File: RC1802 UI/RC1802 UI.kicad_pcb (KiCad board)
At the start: 2 copper layers, 99.1 x 99.1 mm, 65 parts, among them J1 CONN_01X39, J2 BARREL_JACK, J3 Mount, J4 Mount, J5 Mount, J6 Mount, SW1 CLEAR, SW10 IN5, SW11 IN6, SW12 IN7, SW2 IN, SW3 MP, SW4 WAIT, SW5 IN0, SW6 IN1, SW7 IN2, SW8 IN3, SW9 IN4, U1 CDP1802, U10 MC14495P1, U11 28C256, U2 74LS373, U3 HM62256BLP-7, U4 74LS04, U5 4050, U6 4013, U7 74LS10, U8 MC14495P1, U9 74LS245, X1 CXO_DIP14

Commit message: Completed front panel with exports.
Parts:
- removed C10, C11, C8, C9: 100nF, Capacitors_THT:C_Disc_D4.7mm_W2.5mm_P5.00mm
- removed JP1: U12 WE, Pin_Headers:Pin_Header_Straight_1x03_Pitch2.54mm
- removed JP2: Enable, Pin_Headers:Pin_Header_Straight_1x02_Pitch2.54mm
- removed JP3: HI, Pin_Headers:Pin_Header_Straight_1x03_Pitch2.54mm
- removed JP4: LO, Pin_Headers:Pin_Header_Straight_1x03_Pitch2.54mm
- removed R10: 470, Resistors_THT:R_Axial_DIN0207_L6.3mm_D2.5mm_P10.16mm_Horizontal
- removed R4, R5, R6, R7, R8, R9: 47k, Resistors_THT:R_Axial_DIN0207_L6.3mm_D2.5mm_P10.16mm_Horizontal
- removed U10, U8: MC14495P1, Housings_DIP:DIP-16_W7.62mm_Socket
- removed U11: 28C256, Housings_DIP:DIP-32_W15.24mm_Socket
- removed U9: 74LS245, Housings_DIP:DIP-20_W7.62mm_Socket
- removed X1: CXO_DIP14, Oscillators:Oscillator_DIP-14
- J1: value CONN_01X39 -> Mount; footprint Pin_Headers:Pin_Header_Angled_1x39_Pitch2.54mm -> mounting:1pin
- J2: value BARREL_JACK -> Mount; footprint Connectors:BARREL_JACK -> mounting:1pin
- J5: value Mount -> CONN_01X39; footprint mounting:1pin -> Pin_Headers:Pin_Header_Angled_1x39_Pitch2.54mm
- J6: value Mount -> CONN_02X20; footprint mounting:1pin -> Connectors:IDC_Header_Straight_40pins
- R1: value 47k -> 470
- U1: value CDP1802 -> 74LS04; footprint Housings_DIP:DIP-40_W15.24mm_Socket -> Housings_DIP:DIP-14_W7.62mm_Socket
- U2: value 74LS373 -> 4050; footprint Housings_DIP:DIP-20_W7.62mm_Socket -> Housings_DIP:DIP-16_W7.62mm_Socket
- U3: value HM62256BLP-7 -> 4013; footprint Housings_DIP:DIP-32_W15.24mm_Socket -> Housings_DIP:DIP-14_W7.62mm_Socket
- U4: value 74LS04 -> 74LS10
- U5: value 4050 -> MC14495P1
- U6: value 4013 -> 74LS245; footprint Housings_DIP:DIP-14_W7.62mm_Socket -> Housings_DIP:DIP-20_W7.62mm_Socket
- U7: value 74LS10 -> MC14495P1; footprint Housings_DIP:DIP-14_W7.62mm_Socket -> Housings_DIP:DIP-16_W7.62mm_Socket
- moved D4 248.7 mm to (121.3, 101.6), turned to 180 degrees
- moved R1 221.3 mm to (144.8, 107.3), turned to 180 degrees
- moved R3 198.4 mm to (182.2, 123.8), turned to 90 degrees
- moved D3 195.1 mm to (186.1, 113.7), turned to 270 degrees
- moved D6 194.2 mm to (121.3, 104.1), turned to 180 degrees
- moved D2 189.6 mm to (191.8, 113.7), turned to 270 degrees
- moved D7 163.2 mm to (195.6, 113.7), turned to 270 degrees
- moved D5 160.9 mm to (121.3, 99.1), turned to 180 degrees
- moved J5 132.0 mm to (198.1, 146.1), turned to 270 degrees
- moved J6 118.2 mm to (107.3, 132.1), turned to 90 degrees
- moved SW5 112.3 mm to (194.3, 131.4), turned to 270 degrees
- moved J2 108.4 mm to (104.8, 71.8)
- moved SW3 103.8 mm to (117.5, 131.4), turned to 270 degrees
- moved SW6 100.8 mm to (186.1, 131.4), turned to 270 degrees
- moved SW2 92.3 mm to (127.0, 131.4), turned to 270 degrees
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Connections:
- D3 pad 2: WAIT -> ~WAIT
- J1 pad 1: EF1 -> (no net)
- J2 pad 1: VCC -> (no net)
- R1 pad 1: INTERRUPT -> Net-(D1-Pad2)
- R2 pad 1: DMA_OUT -> GND
- R2 pad 2: VCC -> Net-(D3-Pad1)
- R3 pad 1: DMA_IN -> GND
- R3 pad 2: VCC -> LOAD_N2
- SW1 pad 2: CLEAR -> ~CLEAR
- SW3 pad 2: ~WE -> MP
- U1 pad 1: CLOCK -> Net-(D1-Pad1)
- U1 pad 10: /BUS5 -> Net-(D6-Pad2)
- U1 pad 11: /BUS4 -> ~WAIT
- U1 pad 12: /BUS3 -> (no net)
- U1 pad 13: /BUS2 -> (no net)
- U1 pad 14: /BUS1 -> VCC
- U1 pad 2: WAIT -> Q
- U1 pad 3: CLEAR -> Net-(SW2-Pad2)
- U1 pad 4: Q -> /~IN
- U1 pad 5: SC1 -> Net-(D6-Pad2)
- U1 pad 6: SC0 -> ~WAIT
- U1 pad 7: MRD -> GND
- U1 pad 8: /BUS7 -> Net-(SW2-Pad2)
- U1 pad 9: /BUS6 -> /~IN
- U2 pad 1: GND -> VCC
- U2 pad 10: GND -> (no net)
- U2 pad 11: TPA -> (no net)
- U2 pad 12: /MA12 -> (no net)
- U2 pad 13: /MA4 -> (no net)
- U2 pad 14: /MA5 -> (no net)
- U2 pad 15: /MA13 -> (no net)
- U2 pad 16: /MA14 -> (no net)
- U2 pad 2: /MA8 -> ~CLEAR
- U2 pad 3: /MA0 -> ~CLEAR
- U2 pad 4: /MA1 -> STROBE
- U2 pad 5: /MA9 -> Net-(U2-Pad5)
- U2 pad 6: /MA10 -> (no net)
- U2 pad 7: /MA2 -> (no net)
- U2 pad 8: /MA3 -> (no net)
- U2 pad 9: /MA11 -> (no net)
- U3 pad 1: /MA14 -> (no net)
- U3 pad 10: /MA0 -> Net-(D3-Pad1)
- U3 pad 11: /BUS0 -> /~IN
- U3 pad 12: /BUS1 -> Net-(D5-Pad1)
- U3 pad 13: /BUS2 -> (no net)
- U3 pad 14: GND -> VCC
- U3 pad 2: /MA12 -> (no net)
- U3 pad 3: /MA7 -> (no net)
- U3 pad 4: /MA6 -> (no net)
- U3 pad 5: /MA5 -> (no net)
- U3 pad 6: /MA4 -> (no net)
- U3 pad 7: /MA3 -> GND
- U3 pad 8: /MA2 -> GND
- U3 pad 9: /MA1 -> VCC
- U4 pad 1: Net-(D1-Pad1) -> MRD
- U4 pad 10: Net-(D6-Pad2) -> TPB
- U4 pad 11: WAIT -> Net-(U4-Pad11)
- U4 pad 12: Net-(JP3-Pad2) -> Net-(U4-Pad11)
- U4 pad 13: /MA15 -> MRD
- U4 pad 2: Q -> MRD
- U4 pad 3: Net-(SW2-Pad2) -> MRD
- U4 pad 4: /~IN -> LOAD_N2
- U4 pad 5: Net-(D6-Pad2) -> LOAD_N2
- U4 pad 6: WAIT -> READ
- U4 pad 8: Net-(SW2-Pad2) -> Net-(U2-Pad5)
- U4 pad 9: /~IN -> LOAD_N2
- U5 pad 1: VCC -> Net-(AFF1-Pad1)
- U5 pad 10: (no net) -> /BUS4
- U5 pad 12: (no net) -> Net-(AFF1-Pad7)
- U5 pad 13: (no net) -> Net-(AFF1-Pad6)
- U5 pad 14: (no net) -> Net-(AFF1-Pad4)
- U5 pad 15: (no net) -> Net-(AFF1-Pad2)
- U5 pad 16: (no net) -> VCC
- U5 pad 2: CLEAR -> Net-(AFF1-Pad9)
- U5 pad 3: CLEAR -> Net-(AFF1-Pad10)
- U5 pad 4: STROBE -> (no net)
- U5 pad 5: Net-(U5-Pad5) -> /BUS7
- U5 pad 6: (no net) -> /BUS6
- U5 pad 7: (no net) -> STROBE
- U5 pad 8: (no net) -> GND
- U5 pad 9: (no net) -> /BUS5
- U6 pad 1: (no net) -> VCC
- U6 pad 10: Net-(D3-Pad1) -> GND
- U6 pad 11: /~IN -> /BUS7
- U6 pad 12: Net-(D5-Pad1) -> /BUS6
- U6 pad 13: (no net) -> /BUS5
- U6 pad 14: VCC -> /BUS4
- U6 pad 2: (no net) -> Net-(SW5-Pad2)
- U6 pad 3: (no net) -> Net-(SW6-Pad2)
- U6 pad 4: (no net) -> Net-(SW7-Pad2)
- U6 pad 5: (no net) -> Net-(SW8-Pad2)
- U6 pad 6: (no net) -> Net-(SW9-Pad2)
- U6 pad 7: GND -> Net-(SW10-Pad2)
- U6 pad 8: GND -> Net-(SW11-Pad2)
- U6 pad 9: VCC -> Net-(SW12-Pad2)
- U7 pad 1: MRD -> Net-(AFF2-Pad1)
- U7 pad 10: TPB -> /BUS0
- U7 pad 11: Net-(U7-Pad11) -> (no net)
- U7 pad 12: Net-(U7-Pad11) -> Net-(AFF2-Pad7)
- U7 pad 13: MRD -> Net-(AFF2-Pad6)
- U7 pad 14: VCC -> Net-(AFF2-Pad4)
- U7 pad 2: MRD -> Net-(AFF2-Pad9)
- U7 pad 3: MRD -> Net-(AFF2-Pad10)
- U7 pad 4: LOAD_N2 -> (no net)
- U7 pad 5: LOAD_N2 -> /BUS3
- U7 pad 6: READ -> /BUS2
- U7 pad 7: GND -> STROBE
- U7 pad 8: Net-(U5-Pad5) -> GND
- U7 pad 9: LOAD_N2 -> /BUS1
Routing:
- net N2: track 18.4 -> 226.3 mm, vias 0 -> 5
- net ~WAIT: track 0.00 -> 199.1 mm, vias 0 -> 17
- net MRD: track 0.00 -> 196.3 mm, vias 0 -> 8
- net ~CLEAR: track 0.00 -> 182.5 mm, vias 0 -> 12
- net TPB: track 0.00 -> 173.5 mm, vias 0 -> 11
- net SC1: track 0.00 -> 147.3 mm, vias 0 -> 8
- net EF4: track 6.99 -> 153.7 mm, vias 2 -> 9
- net LOAD_N2: track 0.00 -> 133.8 mm, vias 0 -> 4
- net /~IN: track 0.00 -> 106.9 mm, vias 0 -> 7
- net MWR: track 0.00 -> 104.8 mm, vias 0 -> 3
- net Q: track 0.00 -> 101.8 mm, vias 0 -> 7
- net STROBE: track 0.00 -> 97.9 mm, vias 0 -> 6
- net Net-(D3-Pad1): track 0.00 -> 83.7 mm, vias 0 -> 5
- net Net-(SW6-Pad2): track 127.4 -> 50.0 mm, vias 3 -> 0
- net /MA11: track 76.0 -> 0.00 mm, vias 2 -> 0
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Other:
- board size 99.1 x 99.1 mm -> 99.1 x 80 mm
- board text added: "0"
- board text added: "1"
- board text added: "2"
- board text added: "3"
- board text added: "4"
- board text added: "5"
- board text added: "6"
- board text added: "7"
- board text added: "CLEAR"
- board text added: "Front panel connector"
- board text added: "IN"
- board text added: "MP"
- board text added: "RC1802 Cosmac ELF Revision A"
- board text added: "WAIT"

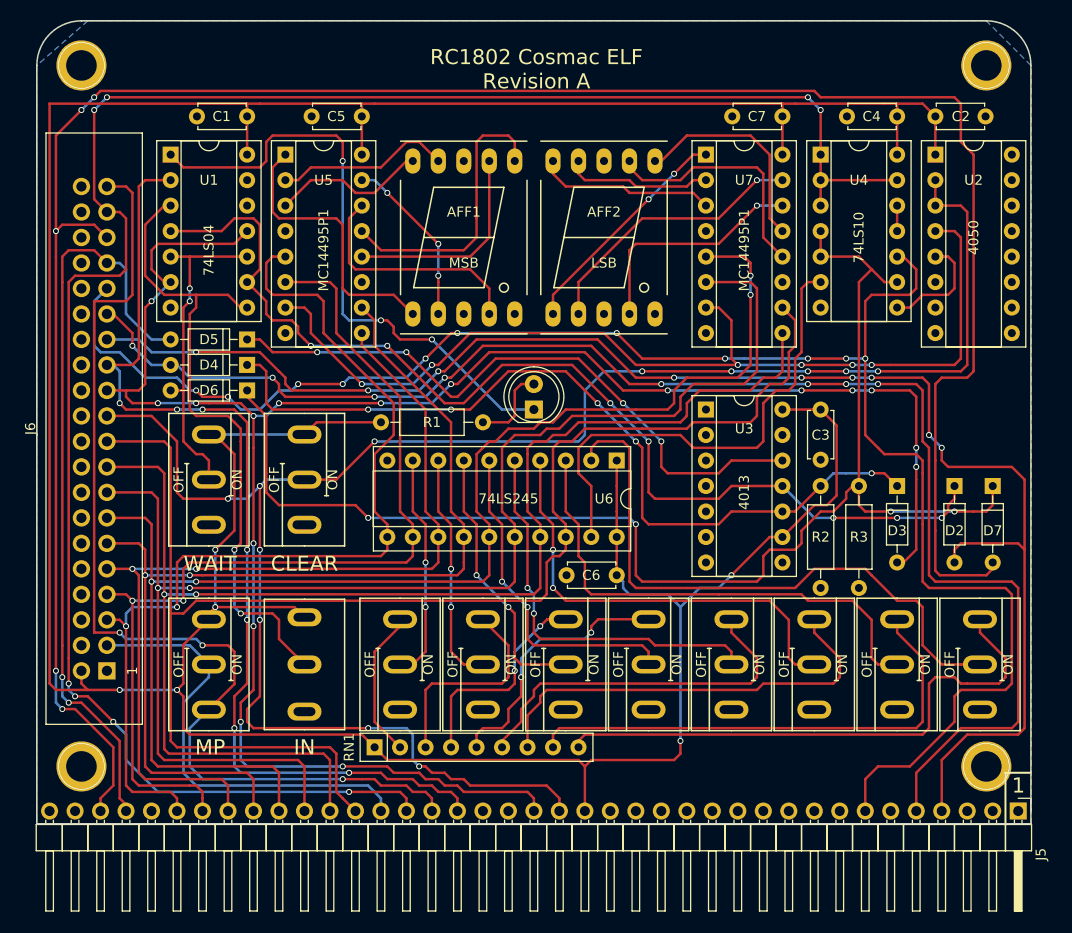
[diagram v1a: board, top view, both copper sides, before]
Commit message: Increased hole sizes for switches
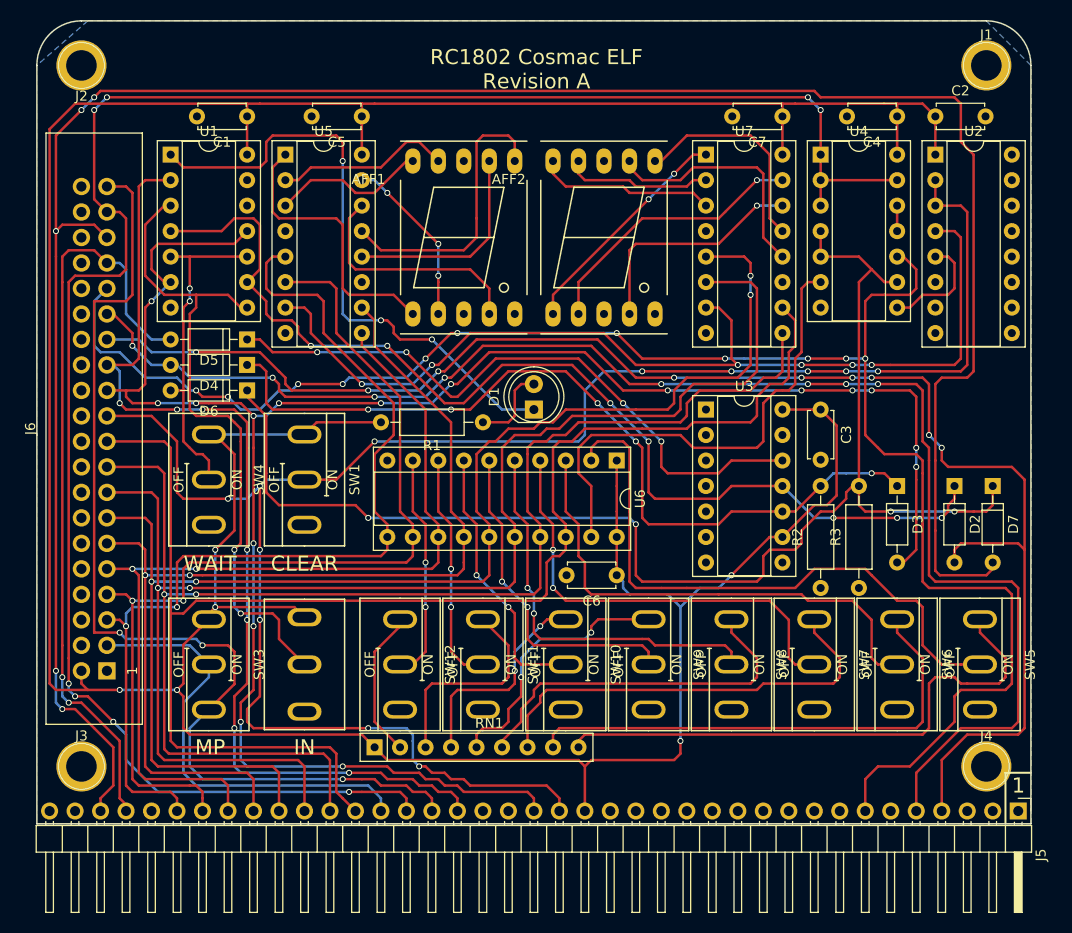
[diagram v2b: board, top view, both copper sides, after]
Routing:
- net VCC: track 370.1 -> 368.6 mm

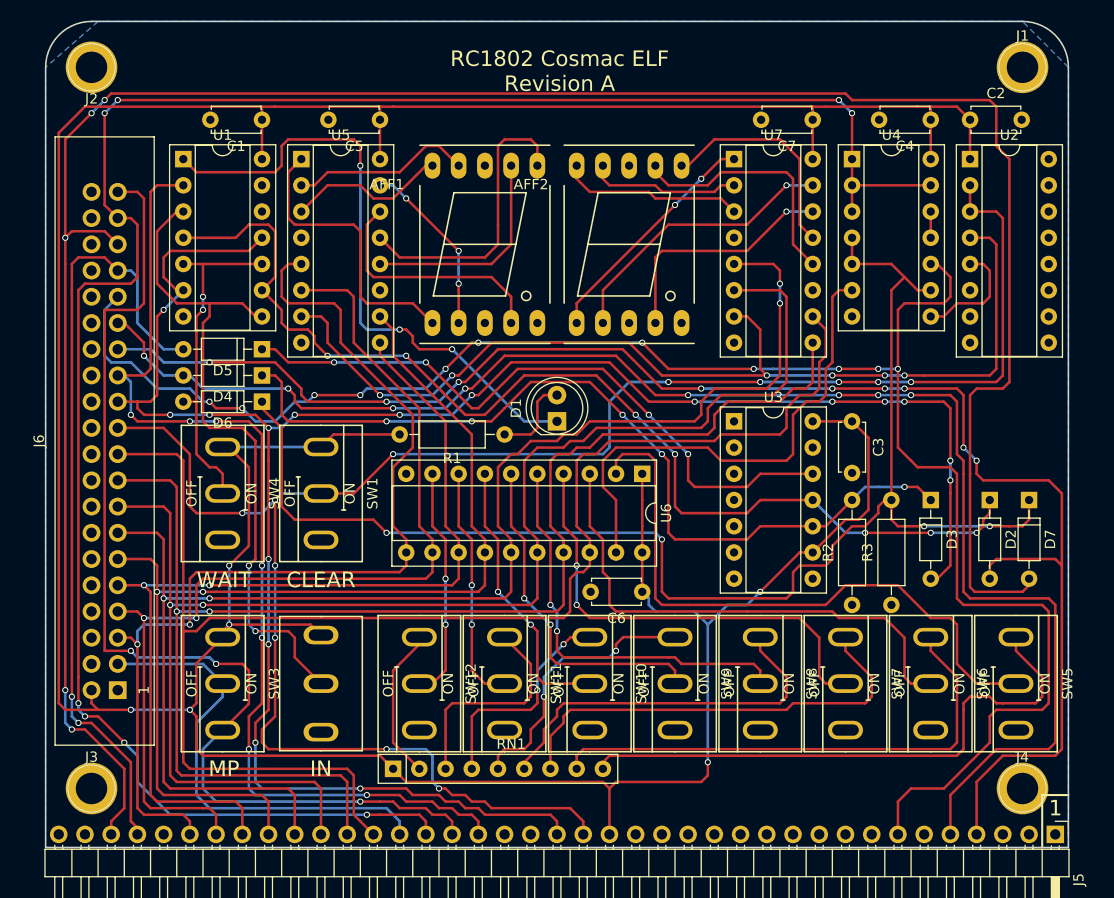
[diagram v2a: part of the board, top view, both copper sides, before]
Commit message: Silkscreen cleanup
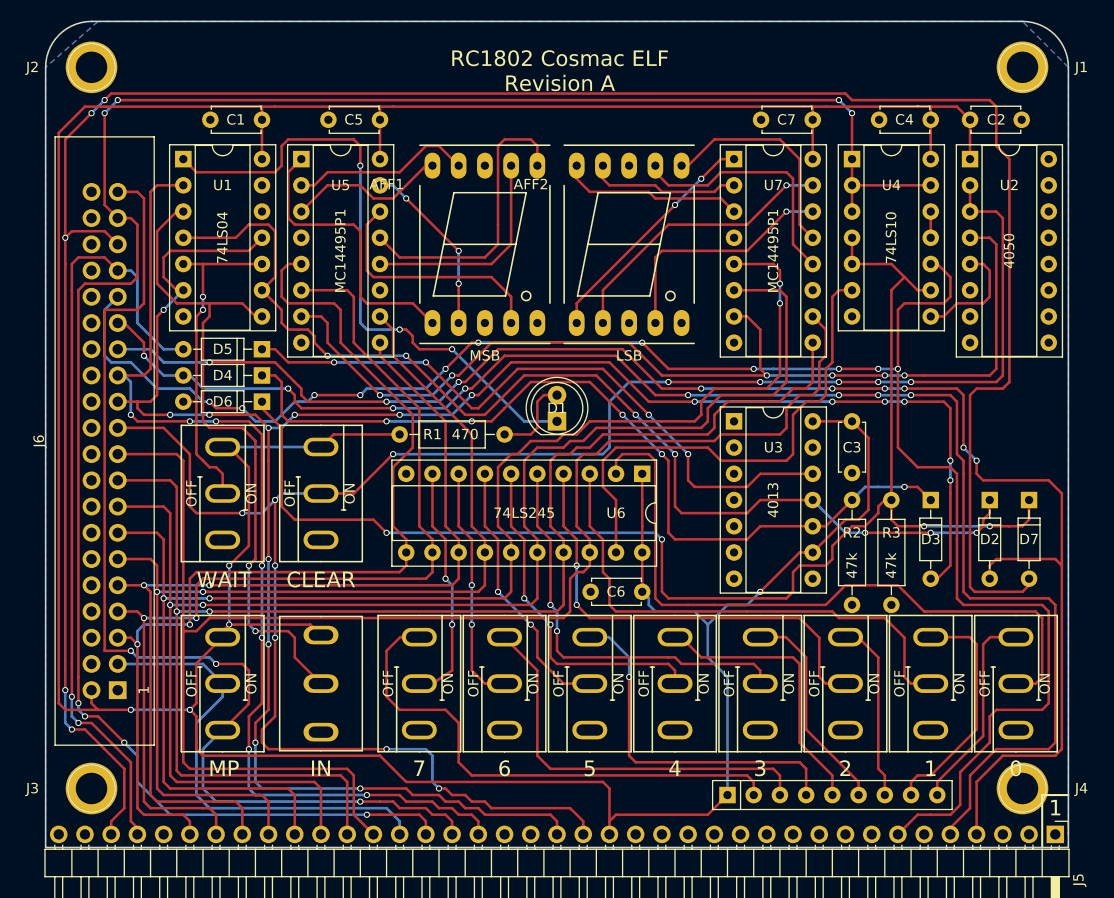
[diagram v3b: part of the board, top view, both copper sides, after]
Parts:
- moved RN1 32.5 mm to (166.4, 142.2)
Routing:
- net Net-(RN1-Pad2): track 14.9 -> 51.3 mm
- net Net-(RN1-Pad9): track 55.8 -> 19.9 mm
- net Net-(RN1-Pad8): track 49.9 -> 22.7 mm
- net Net-(RN1-Pad7): track 43.1 -> 17.6 mm
- net Net-(RN1-Pad3): track 21.3 -> 39.0 mm
- net Net-(RN1-Pad6): track 36.6 -> 20.7 mm
- net Net-(RN1-Pad4): track 21.5 -> 34.4 mm, vias 2 -> 1
- net Net-(SW5-Pad2): track 61.1 -> 67.3 mm
- net VCC: track 368.6 -> 373.7 mm, vias 6 -> 5
- net Net-(SW10-Pad2): track 27.1 -> 26.0 mm
- net Net-(SW12-Pad2): track 22.6 -> 23.4 mm
- net Net-(RN1-Pad5): track 26.5 -> 27.2 mm, vias 2 -> 0

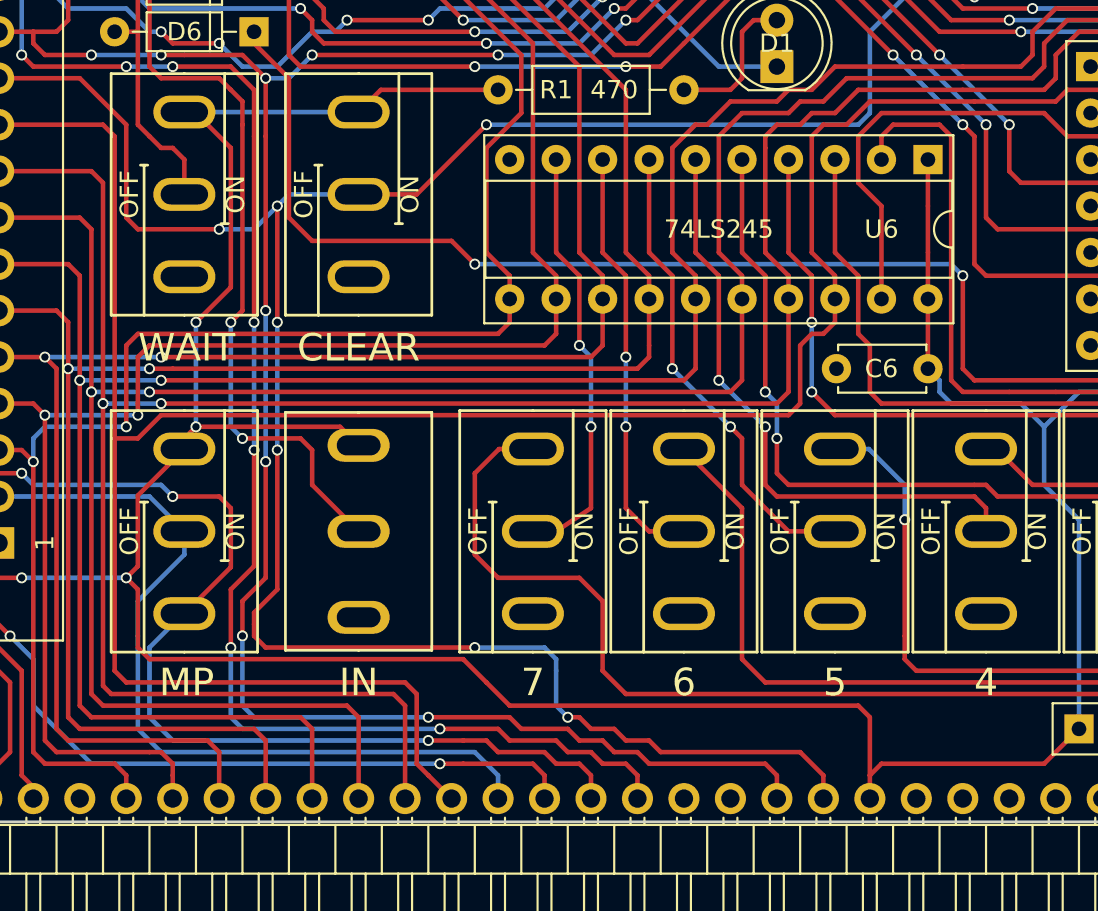
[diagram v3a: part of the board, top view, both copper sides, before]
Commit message: Switched MP and IN
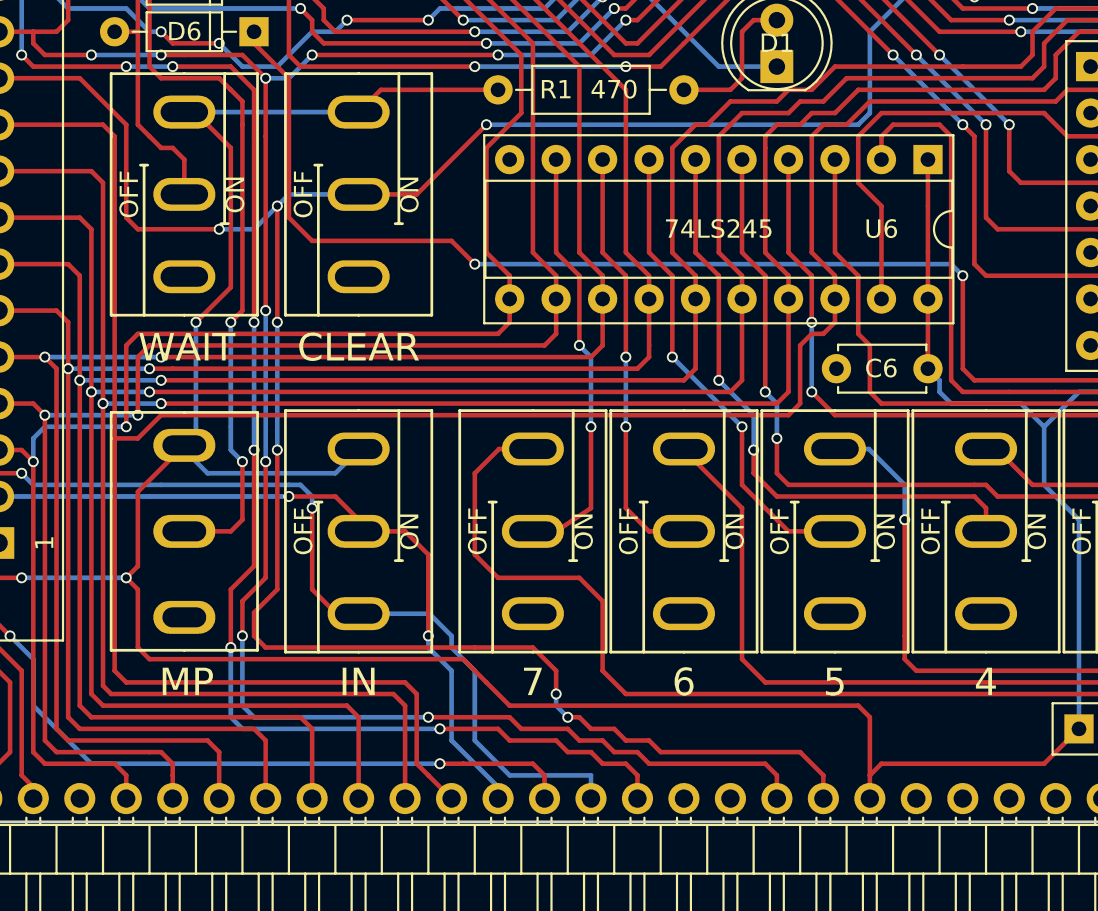
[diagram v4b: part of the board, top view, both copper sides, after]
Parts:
- moved SW2 9.53 mm to (117.5, 131.4)
- moved SW3 9.53 mm to (127.0, 131.4)
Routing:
- net MWR: track 104.8 -> 97.4 mm, vias 3 -> 2
- net MP: track 44.8 -> 40.1 mm, vias 0 -> 2
- net Net-(SW2-Pad2): track 66.0 -> 64.3 mm
- net VCC: track 373.7 -> 375.3 mm, vias 5 -> 4

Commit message: Connected VSS and GND
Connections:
- U2 pad 8: (no net) -> GND
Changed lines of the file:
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@@
 (kicad_pcb (version 4) (host pcbnew 4.0.7)
   (general
-    (links 180)
+    (links 181)
     (no_connects 0)
-    (area 95.375714 67.234999 204.344286 156.825001)
+    (area 100.254999 67.234999 199.465001 147.395001)
     (thickness 1.6)
     (drawings 31)
@@
     (pad 7 thru_hole oval (at 0 15.24) (size 1.6 1.6) (drill 0.8) (layers *.Cu *.Mask))
     (pad 15 thru_hole oval (at 7.62 2.54) (size 1.6 1.6) (drill 0.8) (layers *.Cu *.Mask))
-    (pad 8 thru_hole oval (at 0 17.78) (size 1.6 1.6) (drill 0.8) (layers *.Cu *.Mask))
+    (pad 8 thru_hole oval (at 0 17.78) (size 1.6 1.6) (drill 0.8) (layers *.Cu *.Mask)
+      (net 3 GND))
     (pad 16 thru_hole oval (at 7.62 0) (size 1.6 1.6) (drill 0.8) (layers *.Cu *.Mask))
     (model ${KISYS3DMOD}/Housings_DIP.3dshapes/DIP-16_W7.62mm_Socket.wrl

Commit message: Removed backplane connector and cleanup
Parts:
- removed J5: CONN_01X39, Pin_Headers:Pin_Header_Angled_1x39_Pitch2.54mm
- moved RN1 2.54 mm to (166.4, 144.8)
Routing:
- net SC1: track 147.3 -> 9.83 mm, vias 8 -> 1
- net MRD: track 196.3 -> 99.8 mm, vias 8 -> 4
- net Q: track 101.8 -> 24.7 mm, vias 7 -> 0
- net TPB: track 173.5 -> 105.6 mm
- net ~WAIT: track 199.1 -> 132.2 mm, vias 17 -> 13
- net DMA_IN: track 76.0 -> 12.1 mm, vias 2 -> 0
- net N2: track 226.3 -> 162.6 mm, vias 5 -> 2
- net ~CLEAR: track 182.1 -> 121.5 mm, vias 12 -> 7
- net /BUS1: track 140.8 -> 103.4 mm
- net /BUS0: track 149.2 -> 112.9 mm
- net /BUS2: track 142.9 -> 106.8 mm
- net /BUS3: track 138.3 -> 103.5 mm
- net /BUS4: track 102.4 -> 68.9 mm
- net /BUS5: track 91.8 -> 59.3 mm
- net EF4: track 153.7 -> 121.3 mm
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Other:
- board text added: "RC1802 Cosmac ELF Revision B"
- board text added: "https://hvetebolle.blogspot.com"
- board text removed: "RC1802 Cosmac ELF Revision A"
